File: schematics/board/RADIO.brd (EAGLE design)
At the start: 76 x 76 mm, 47 parts, among them X2 AKKUM

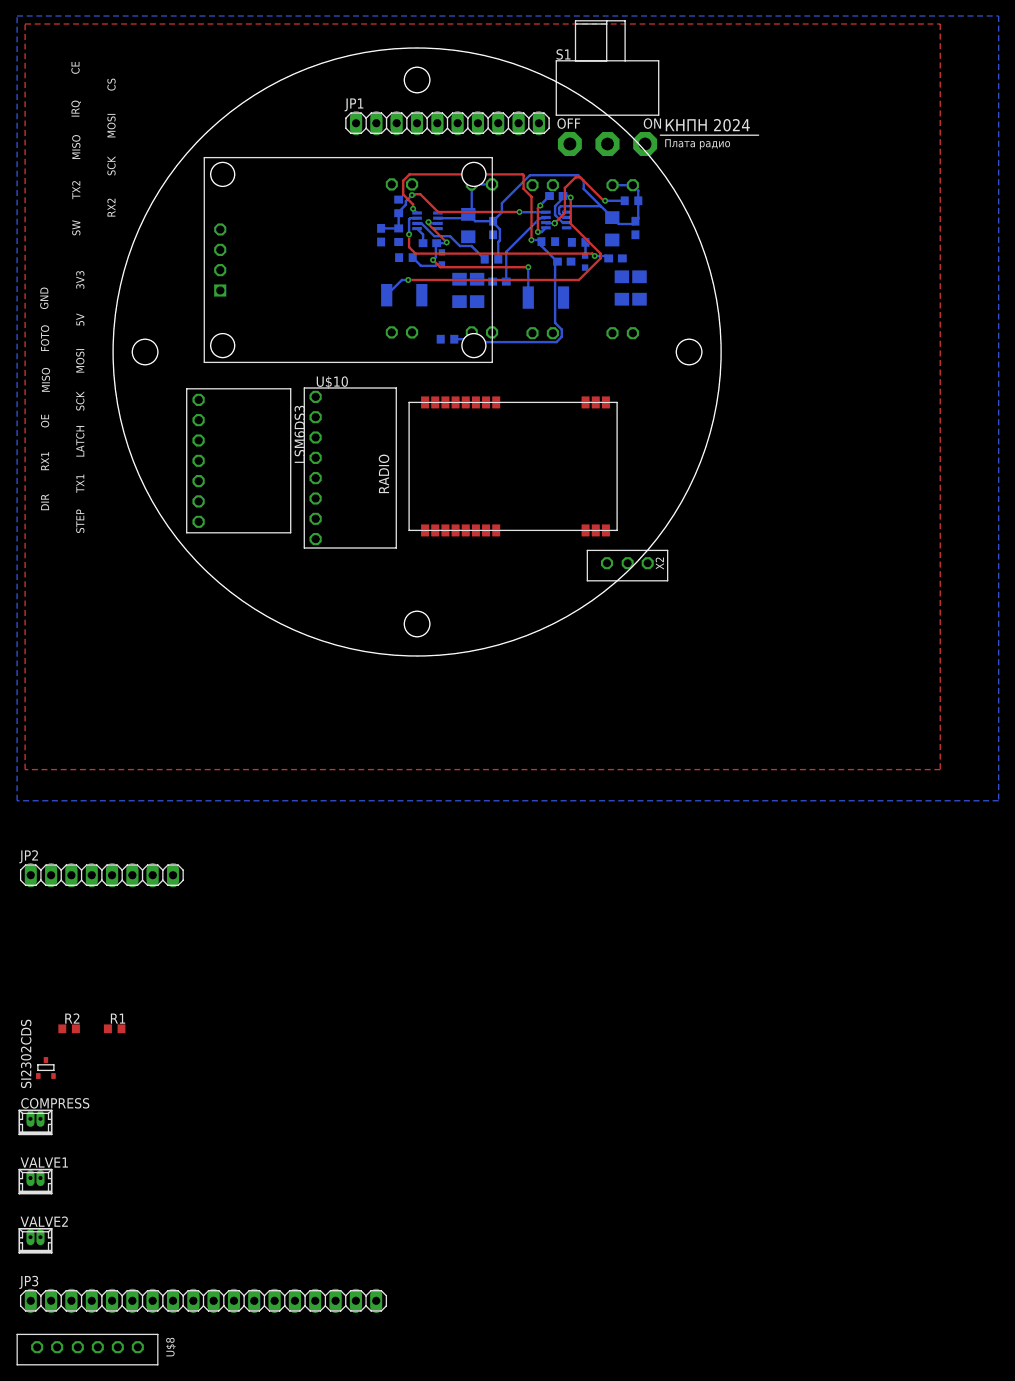
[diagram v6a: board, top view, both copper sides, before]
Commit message: распиновка разъемов плат
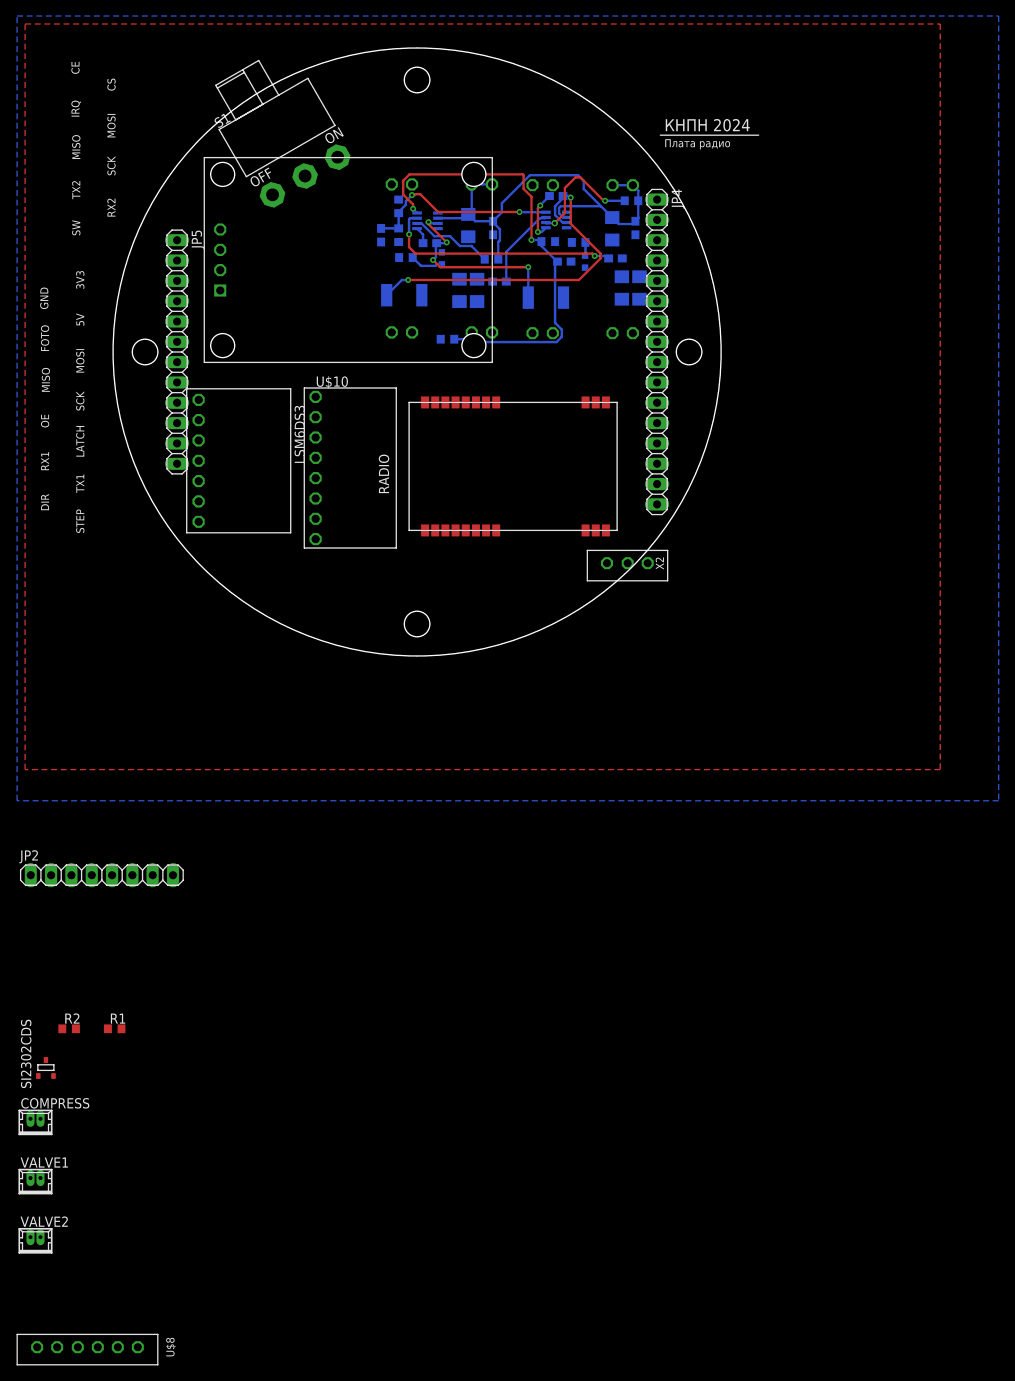
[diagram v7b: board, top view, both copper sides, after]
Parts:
- removed JP1: (no value), pinhead:1X10
- removed JP3: (no value), pinhead:1X18
- added JP4: (no value), pinhead:1X16
- added JP5: (no value), pinhead:1X12
- moved S1 38.0 mm to (36.0, 72.0), turned to 30 degrees
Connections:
- net 3V3: now also JP5.3; no longer JP3.6
- net 4V: now also JP5.1; no longer JP1.10
- net 5V: now also JP5.4; no longer JP3.7
- net AUX_RADIO: now also JP5.7; no longer JP3.10
- net C0: now also JP4.13; no longer JP3.1
- net CS_LIS: now also JP4.9; no longer JP1.8
- net CS_LSM: now also JP4.10; no longer JP1.9
- net GERMO: now also JP5.6; no longer JP3.18
- net GND: now also JP5.2; no longer JP3.5
- net LATCH_SR: now also JP4.12; no longer JP1.5
- net M0_RADIO: now also JP5.9; no longer JP3.12
- net M1_RADIO: now also JP5.8; no longer JP3.11
- net MICS: now also JP4.16; no longer JP3.4
- net MISO_SENS: now also JP4.4; no longer JP1.2
- net MOSI_SENS: now also JP4.3; no longer JP1.1
- net NH3: now also JP4.15; no longer JP3.3
- net NO2: now also JP4.14; no longer JP3.2
- net OE_SR: now also JP4.11; no longer JP1.4
- net RX_GPS: now also JP5.11; no longer JP3.14
- net RX_LIDAR: now also JP4.7; no longer JP3.15
- net RX_RADIO: now also JP4.5; no longer JP1.6
- net SCK_SENS: now also JP5.12; no longer JP1.3
- net SCL: now also JP4.2; no longer JP3.9
- net SDA: now also JP4.1; no longer JP3.8
- net SHIFT: now also JP5.5; no longer JP3.17
- net TX_GPS: now also JP5.10; no longer JP3.13
- net TX_LIDAR: now also JP4.8; no longer JP3.16
- net TX_RADIO: now also JP4.6; no longer JP1.7

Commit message: длорпамсвч
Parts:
- moved S1 14.4 mm to (24.0, 64.0), turned to 60 degrees
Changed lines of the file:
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@@
 <?xml version="1.0" encoding="utf-8"?>
 <!DOCTYPE eagle SYSTEM "eagle.dtd">
-<eagle version="9.4.2">
+<eagle version="9.6.2">
 <drawing>
 <settings>
-<setting alwaysvectorfont="yes"/>
+<setting alwaysvectorfont="no"/>
 <setting verticaltext="up"/>
 </settings>
@@
 <attribute name="VALUE" x="37.32" y="24.07" size="1.27" layer="27"/>
 </element>
-<element name="S1" library="UNKNOWN-2024" package="SS_12D11" value="" x="36" y="72" smashed="yes" rot="R30">
-<attribute name="NAME" x="25.111884375" y="77.902759375" size="1.27" layer="25" ratio="10" rot="R30"/>
-<attribute name="VALUE" x="30.721996875" y="81.141759375" size="1.27" layer="27" ratio="10" rot="R30"/>
+<element name="S1" library="UNKNOWN-2024" package="SS_12D11" value="" x="24" y="64" smashed="yes" rot="R60">
+<attribute name="NAME" x="11.61923125" y="63.66788125" size="1.27" layer="25" ratio="10" rot="R60"/>
+<attribute name="VALUE" x="14.85823125" y="69.27799375" size="1.27" layer="27" ratio="10" rot="R60"/>
 </element>
 <element name="X2" library="UNKNOWN-2024" package="JST-3-2.5" value="AKKUM" x="76.3" y="23.6" smashed="yes">
@@
 <contactref element="S1" pad="2"/>
 <wire x1="77.11370625" y1="66" x2="77.3" y2="66.35" width="0" layer="19" extent="16-16"/>
-<wire x1="36" y1="72" x2="60.15" y2="61.6" width="0" layer="19" extent="16-16"/>
+<wire x1="24" y1="64" x2="52.6" y2="66.725" width="0" layer="19" extent="16-16"/>
 </signal>
 <signal name="N$9">
@@
 <contactref element="X2" pad="1"/>
 <contactref element="S1" pad="3"/>
-<wire x1="40.07031875" y1="74.35" x2="78.82" y2="23.6" width="0" layer="19" extent="1-1"/>
+<wire x1="26.35" y1="68.07031875" x2="78.82" y2="23.6" width="0" layer="19" extent="1-1"/>
 </signal>
 <signal name="RX_GPS">
